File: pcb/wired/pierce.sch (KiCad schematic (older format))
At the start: 30 parts, among them SW11 SW_PUSH, SW12 SW_PUSH, SW13 SW_PUSH, SW14 SW_PUSH, SW19 SW_PUSH, SW20 SW_PUSH, SW21 SW_PUSH, SW22 SW_PUSH, SW27 SW_PUSH, SW28 SW_PUSH, SW29 SW_PUSH, SW34 SW_PUSH, SW35 SW_PUSH, SW36 SW_PUSH, SW4 SW_PUSH, SW5 SW_PUSH, SW6 SW_PUSH, SW7 SW_PUSH

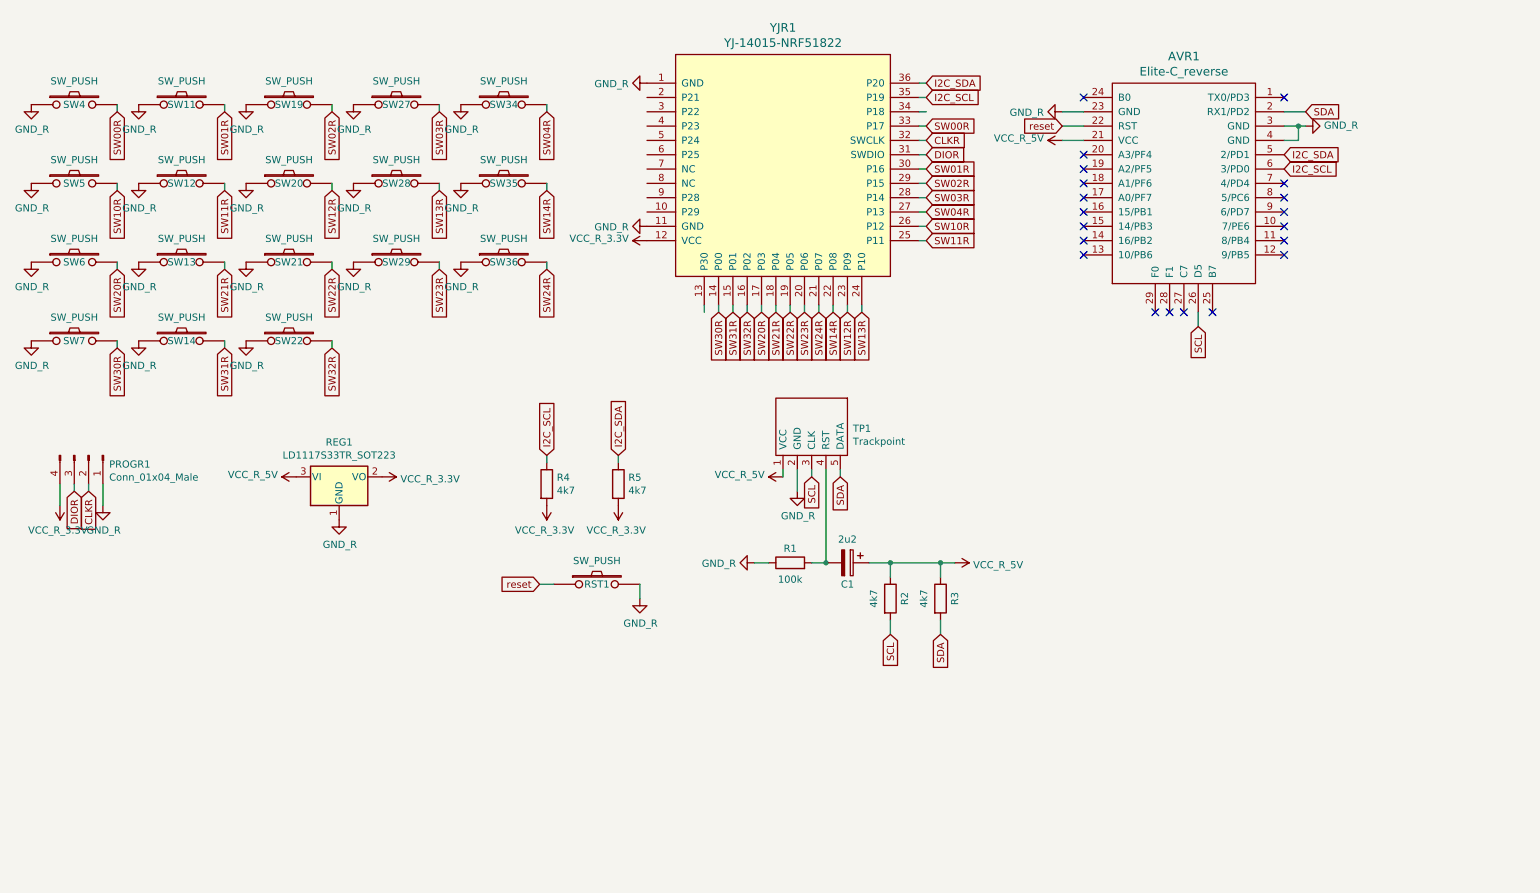
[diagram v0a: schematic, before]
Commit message: add reciever pcb for dual wireless setup
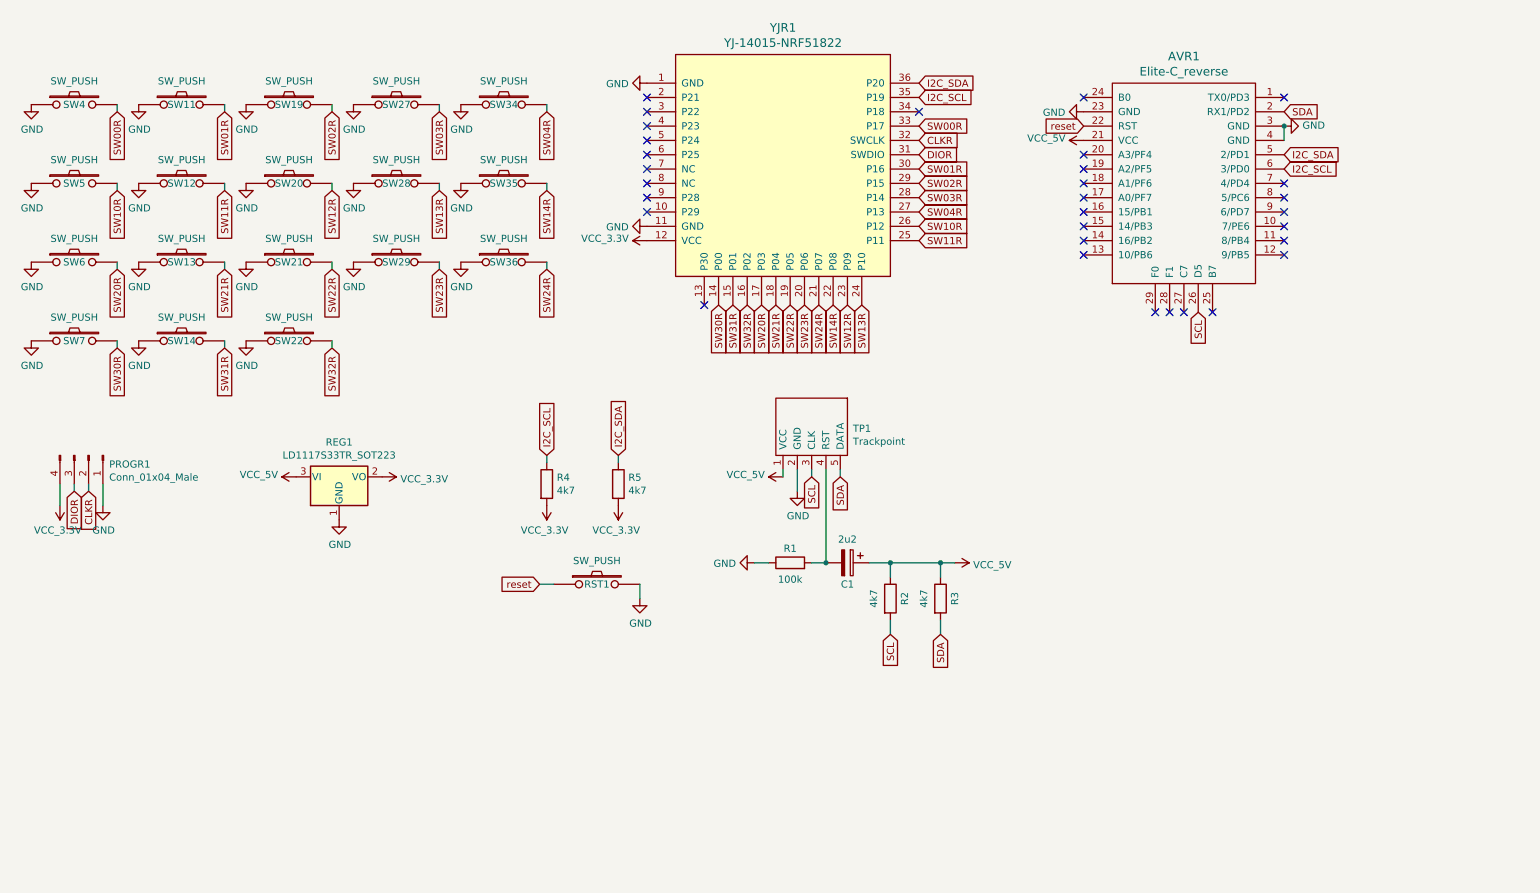
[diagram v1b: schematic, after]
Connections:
- net GND_R renamed GND
- net VCC_R_3.3V renamed VCC_3.3V
- net VCC_R_5V renamed VCC_5V
- no-connect marks 20 -> 31

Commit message: small adjustments
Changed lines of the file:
@@
 encoding utf-8
 Sheet 1 1
-Title "pierce keyboard - wired"
+Title "pierce keyboard - wired side"
 Date "2021-06-16"
 Rev "v 2.0"
@@
 Text GLabel 8850 2650 3    50   Input ~ 0
 SCL
-Text GLabel 6350 3800 3    50   Input ~ 0
+Text GLabel 6350 3750 3    50   Input ~ 0
 SDA
-Text GLabel 6150 3800 3    50   Input ~ 0
+Text GLabel 6150 3750 3    50   Input ~ 0
 SCL
-Wire Wire Line
-	6150 3800 6150 3750
-Wire Wire Line
-	6350 3800 6350 3750
 Wire Wire Line
 	5850 4400 5750 4400
@@
 	7150 4400 7050 4400
 Connection ~ 7050 4400
-$Comp
-L pierce:Trackpoint TP1
-U 1 1 60324084
-P 6150 3400
-F 0 "TP1" V 6212 3688 50  0000 L CNN
-F 1 "Trackpoint" V 6303 3688 50  0000 L CNN
-F 2 "pierce:TRACKPOINT" H 6150 3400 50  0001 C CNN
-F 3 "" H 6150 3400 50  0001 C CNN
-	1    6150 3400
-	0    1    1    0
-$EndComp
 $Comp
 L pierce:Elite-C_reverse AVR1
@@
 	0    1    1    0
 $EndComp
-Text GLabel 1100 3900 3    50   Input ~ 0
+Text GLabel 1100 3850 3    50   Input ~ 0
 CLKR
-Text GLabel 1000 3900 3    50   Input ~ 0
+Text GLabel 1000 3850 3    50   Input ~ 0
 DIOR
 $Comp
@@
 	1    0    0    -1
 $EndComp
-Wire Wire Line
-	1000 3900 1000 3850
-Wire Wire Line
-	1100 3850 1100 3900
-Wire Wire Line
-	5950 3800 5950 3750
-Wire Wire Line
-	900  4000 900  3850
-Wire Wire Line
-	1200 3850 1200 4000
 Text GLabel 6900 1050 2    50   Input ~ 0
 I2C_SDA
@@
 	1    0    0    -1
 $EndComp
-Text GLabel 4300 3650 1    50   Input ~ 0
+Text GLabel 4300 3700 1    50   Input ~ 0
 I2C_SCL
-Text GLabel 4800 3650 1    50   Input ~ 0
+Text GLabel 4800 3700 1    50   Input ~ 0
 I2C_SDA
 $Comp
@@
 	1    0    0    -1
 $EndComp
-Wire Wire Line
-	4300 3700 4300 3650
-Wire Wire Line
-	4800 3650 4800 3700
 NoConn ~ 8050 1150
 NoConn ~ 8050 1550
@@
 NoConn ~ 9450 1750
 NoConn ~ 9450 1150
-Wire Wire Line
-	6050 3750 6050 3900
 Text GLabel 6400 2600 3    50   Input ~ 0
 SW12R
@@
 L power:GND #PWR?
 U 1 1 60E3728E
-P 6050 3900
-F 0 "#PWR?" H 6050 3650 50  0001 C CNN
-F 1 "GND" H 6055 3727 50  0000 C CNN
-F 2 "" H 6050 3900 50  0001 C CNN
-F 3 "" H 6050 3900 50  0001 C CNN
-	1    6050 3900
+P 6050 3750
+F 0 "#PWR?" H 6050 3500 50  0001 C CNN
+F 1 "GND" V 6050 3550 50  0000 C CNN
+F 2 "" H 6050 3750 50  0001 C CNN
+F 3 "" H 6050 3750 50  0001 C CNN
+	1    6050 3750
 	1    0    0    -1
 $EndComp
@@
 L power:GND #PWR?
 U 1 1 60E45ECE
-P 1200 4000
-F 0 "#PWR?" H 1200 3750 50  0001 C CNN
-F 1 "GND" H 1205 3827 50  0000 C CNN
-F 2 "" H 1200 4000 50  0001 C CNN
-F 3 "" H 1200 4000 50  0001 C CNN
-	1    1200 4000
+P 1200 3850
+F 0 "#PWR?" H 1200 3600 50  0001 C CNN
+F 1 "GND" V 1200 3650 50  0000 C CNN
+F 2 "" H 1200 3850 50  0001 C CNN
+F 3 "" H 1200 3850 50  0001 C CNN
+	1    1200 3850
 	1    0    0    -1
 $EndComp
@@
 L pierce:VCC_5V #PWR?
 U 1 1 60E669AB
-P 5950 3800
-F 0 "#PWR?" H 5950 3650 50  0001 C CNN
-F 1 "VCC_5V" V 5965 3927 50  0000 L CNN
-F 2 "" H 5950 3800 50  0001 C CNN
-F 3 "" H 5950 3800 50  0001 C CNN
-	1    5950 3800
-	0    -1   -1   0
+P 5950 3750
+F 0 "#PWR?" H 5950 3600 50  0001 C CNN
+F 1 "VCC_5V" V 5965 3877 50  0000 L CNN
+F 2 "" H 5950 3750 50  0001 C CNN
+F 3 "" H 5950 3750 50  0001 C CNN
+	1    5950 3750
+	-1   0    0    1
 $EndComp
 $Comp
@@
 L pierce:VCC_3.3V #PWR?
 U 1 1 60E842A4
-P 900 4000
-F 0 "#PWR?" H 900 3850 50  0001 C CNN
-F 1 "VCC_3.3V" H 915 4173 50  0000 C CNN
-F 2 "" H 900 4000 50  0001 C CNN
-F 3 "" H 900 4000 50  0001 C CNN
-	1    900  4000
+P 900 3850
+F 0 "#PWR?" H 900 3700 50  0001 C CNN
+F 1 "VCC_3.3V" V 900 4150 50  0000 C CNN
+F 2 "" H 900 3850 50  0001 C CNN
+F 3 "" H 900 3850 50  0001 C CNN
+	1    900  3850
 	-1   0    0    1
 $EndComp
@@
 NoConn ~ 5000 1950
 NoConn ~ 5400 2600
+$Comp
+L pierce:Trackpoint TP1
+U 1 1 60324084
+P 6150 3400
+F 0 "TP1" V 6212 3688 50  0000 L CNN
+F 1 "Trackpoint" V 6303 3688 50  0000 L CNN
+F 2 "pierce:TRACKPOINT" H 6150 3400 50  0001 C CNN
+F 3 "" H 6150 3400 50  0001 C CNN
+	1    6150 3400
+	0    1    1    0
+$EndComp
 $EndSCHEMATC

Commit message: schematic done, started place & route
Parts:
- removed AVR1: Elite-C_reverse, pierce:Elite-C_reverse_D5, symbol pierce:Elite-C_reverse
- added C2, C5: 22p, Capacitor_SMD:C_0805_2012Metric_Pad1.18x1.45mm_HandSolder, symbol Device:C_Small
- added C3, C4, C6, C7: 100n, Capacitor_SMD:C_0805_2012Metric_Pad1.18x1.45mm_HandSolder, symbol Device:C_Small
- added C8: 10u, Capacitor_SMD:C_0805_2012Metric_Pad1.18x1.45mm_HandSolder, symbol Device:C_Small
- added C9: 1u, Capacitor_SMD:C_0805_2012Metric_Pad1.18x1.45mm_HandSolder, symbol Device:C_Small
- added F1: 500m, Fuse:Fuse_0805_2012Metric_Pad1.15x1.40mm_HandSolder, symbol Device:Polyfuse_Small
- added J1: AVR-ISP-6, random-keyboard-parts:Reset_Pretty-Mask, symbol Connector:AVR-ISP-6
- added R10, R11: 10k, Resistor_SMD:R_0805_2012Metric_Pad1.20x1.40mm_HandSolder, symbol Device:R_Small
- added R6, R7: 5.1k, Resistor_SMD:R_0805_2012Metric_Pad1.20x1.40mm_HandSolder, symbol Device:R_Small
- added R8, R9: 22, Resistor_SMD:R_0805_2012Metric_Pad1.20x1.40mm_HandSolder, symbol Device:R_Small
- added U1: PRTR5V0U2X, random-keyboard-parts:SOT143B, symbol pierce:PRTR5V0U2X
- added U2: ATmega32U4-AU, Package_QFP:TQFP-44_10x10mm_P0.8mm, symbol MCU_Microchip_ATmega:ATmega32U4-AU
- added USB1: HRO-TYPE-C-31-M-12, Type-C:HRO-TYPE-C-31-M-12-HandSoldering, symbol Type-C:HRO-TYPE-C-31-M-12
- added Y1: XTAL, Crystal:Crystal_SMD_3225-4Pin_3.2x2.5mm_HandSoldering, symbol Device:Crystal_GND24_Small
- C1: footprint pierce:C_SMD_v2 -> Capacitor_SMD:C_0805_2012Metric_Pad1.18x1.45mm_HandSolder; symbol Device:CP -> pierce-rescue:CP-Device
- PROGR1: symbol Connector:Conn_01x04_Male -> pierce-rescue:Conn_01x04_Male-Connector
- R1, R2, R3, R4, R5: footprint pierce:R_SMD_v2 -> Resistor_SMD:R_0805_2012Metric_Pad1.20x1.40mm_HandSolder; symbol Device:R -> pierce-rescue:R-Device
- REG1: footprint Package_TO_SOT_SMD:SOT-223-3_TabPin2 -> Package_TO_SOT_SMD:SOT-223; symbol Regulator_Linear:LD1117S33TR_SOT223 -> pierce-rescue:LD1117S33TR_SOT223-Regulator_Linear
- SW11, SW12, SW13, SW14, SW19, SW20, SW21, SW22, SW27, SW28, SW29, SW34, SW35, SW36, SW4, SW5, SW6, SW7: footprint kbd:CherryMX_ChocV2_1u -> kbd:MX_ALPS_PG1350_noLed
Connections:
- net GND: now also C2.2, C3.2, C4.2, C5.2, C6.2, C7.2, C8.2, C9.2, J1.6 (GND), R11.1, R6.1, R7.1, U1.1 (GND), U2.15 (GND), U2.23 (GND), U2.35 (GND), U2.43 (GND), U2.5 (UGND), USB1.1 (GND), USB1.12 (GND), USB1.13 (SHIELD), Y1.2, Y1.4
- net I2C_SCL: now also U2.18 (PD0)
- net I2C_SDA: now also U2.19 (PD1)
- net SCL: now also U2.22 (PD5)
- net SDA: now also U2.20 (PD2)
- net VCC_5V: now also C3.1, C4.1, C6.1, C7.1, C8.1, F1.1, J1.2 (VCC), R10.2, U2.14 (VCC), U2.2 (UVCC), U2.24 (AVCC), U2.34 (VCC), U2.44 (AVCC), U2.7 (VBUS)
- net reset: now also J1.5 (~RST), R10.1, U2.13 (~RESET)
- new net: C9.1, U2.6 (UCAP)
- new net: R11.2, U2.33 (~HWB~/PE2)
- new net: R6.2, USB1.10 (CC2)
- new net: R7.2, USB1.4 (CC1)
- new net: R8.2, USB1.5 (DN2), USB1.7 (DN1)
- new net: R9.2, USB1.6 (DP1), USB1.8 (DP2)
- new net D+: R9.1, U1.2 (IO1), U2.4 (D+)
- new net D-: R8.1, U1.3 (IO2), U2.3 (D-)
- new net MISO: J1.1 (MISO), U2.11 (PB3)
- new net MOSI: J1.4 (MOSI), U2.10 (PB2)
- new net SCK: J1.3 (SCK), U2.9 (PB1)
- new net VCC: F1.2, U1.4 (VCC), USB1.11 (VBUS), USB1.2 (VBUS)
- new net XTAL1: C2.1, U2.17 (XTAL1), Y1.1
- new net XTAL2: C5.1, U2.16 (XTAL2), Y1.3
- no-connect marks 31 -> 33
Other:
- moved on the sheet: C1, R1, R2, R3, R4, R5, RST1, TP1
